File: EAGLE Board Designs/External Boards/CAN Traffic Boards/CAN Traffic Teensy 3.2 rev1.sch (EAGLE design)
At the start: 7 parts, among them X1 CONNECTOR-4NANO-FIT_RIGHT_ANG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

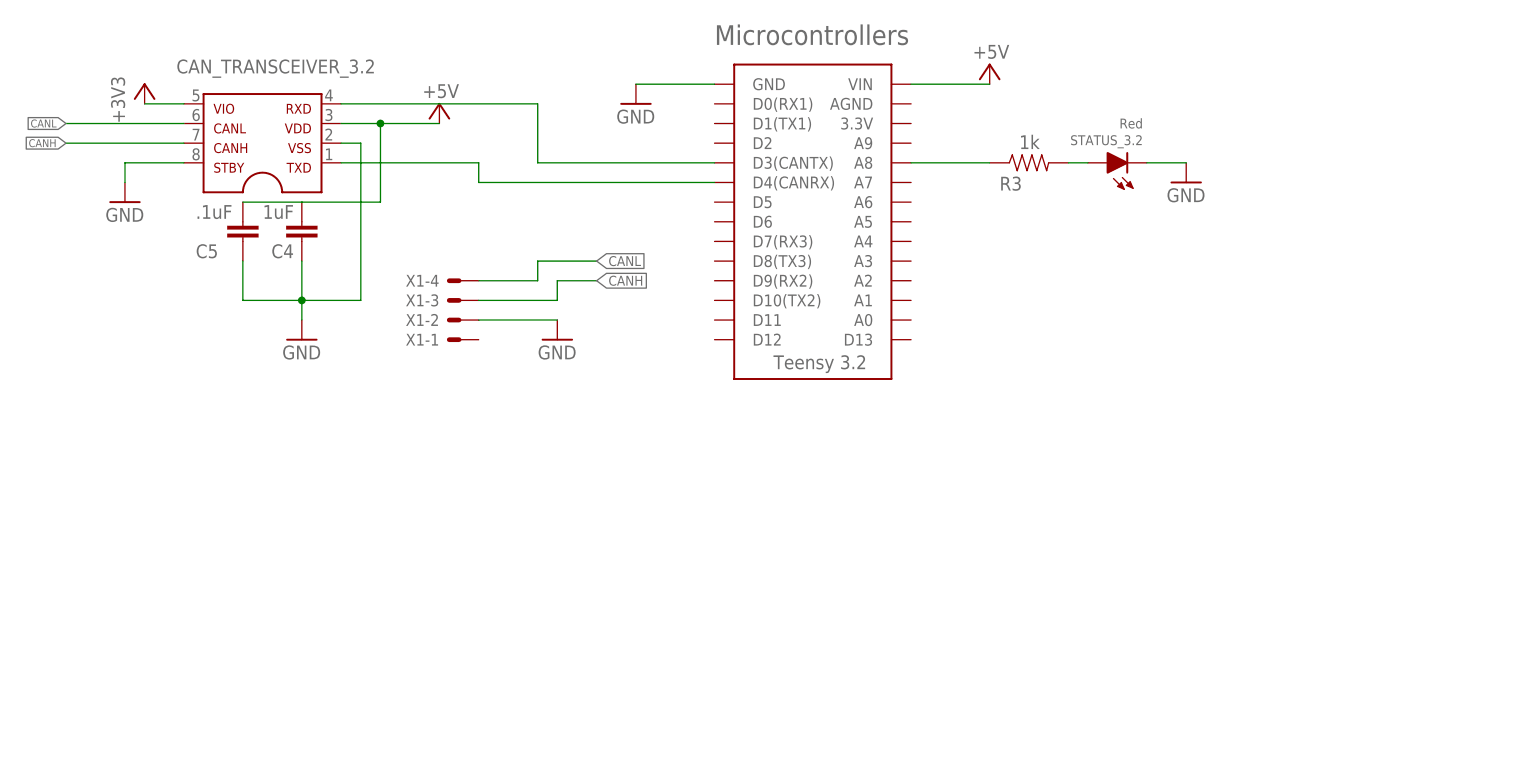
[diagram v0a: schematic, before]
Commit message: CAN Transceiver Boards
Added CAN Termination resistors, remade boards, added labels, put all LEDs on the same pin, added silksreens, and switched LED packages.
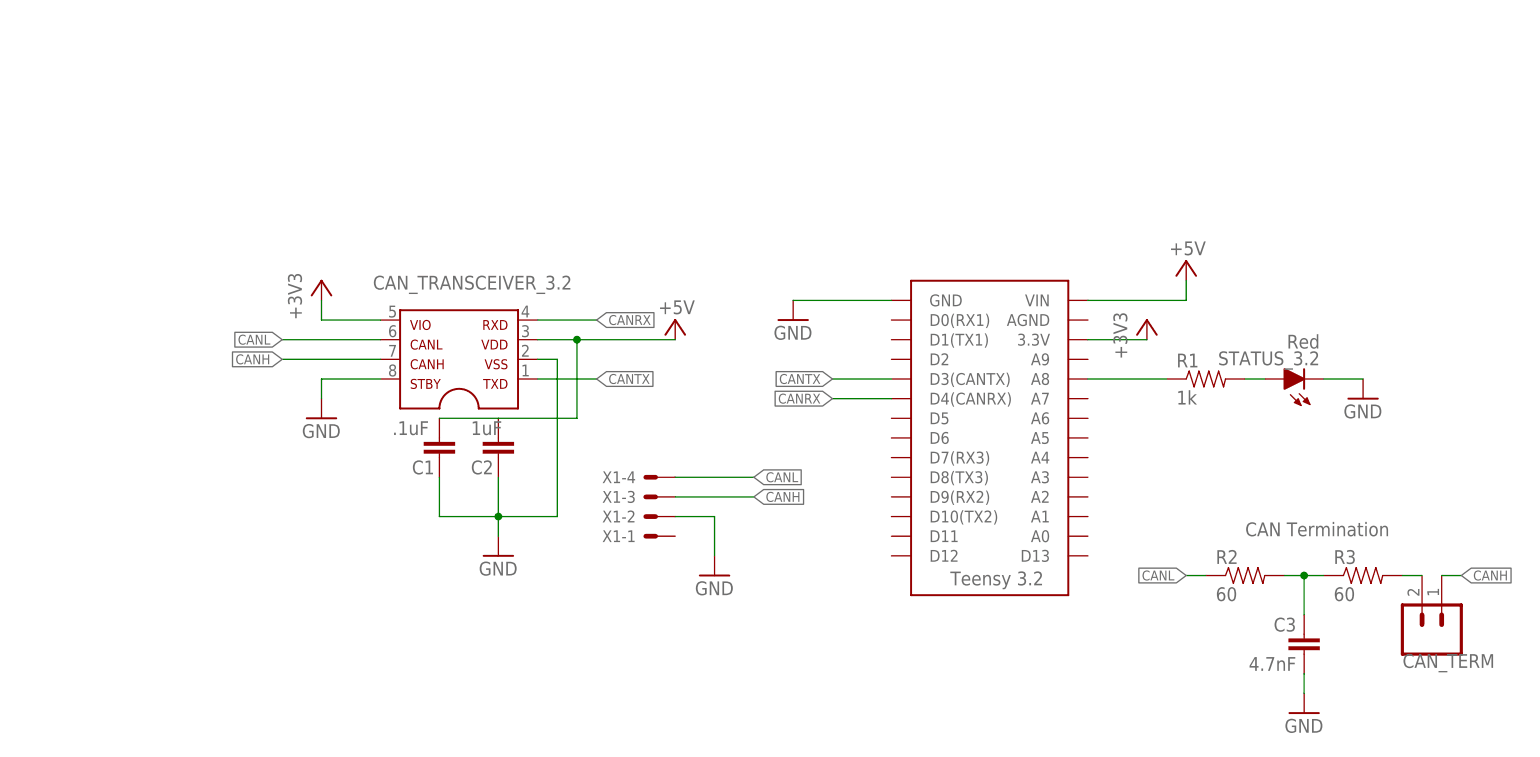
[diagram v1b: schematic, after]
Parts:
- removed C4: 1uF, HyTechDevices:CAP0603-CAP
- removed C5: .1uF, HyTechDevices:CAP0603-CAP
- removed U$1: TEENSY_3.2_SIMPLE, HyTechDevices:TEENSY_3.2_SIMPLE
- added 3.2: TEENSY_3.2_SIMPLE, HyTechDevices:TEENSY_3.2_SIMPLE
- added C1: .1uF, HyTechDevices:CAP0603-CAP
- added C2: 1uF, HyTechDevices:CAP0603-CAP
- added C3: 4.7nF, HyTechDevices:CAP0603-CAP
- added CAN_TERM: M02_SLIM, HyTechDevices:M02_SLIM
- added R1: 1k, HyTechDevices:RESISTOR0603-RES
- added R2: 60, HyTechDevices:RESISTOR0603-RES
- CAN_TRANSCEIVER_3.2: value MCP2562SOIC-08 -> MCP2562FDSOIC-08; device HyTechDevices:MCP2562SOIC-08 -> HyTechDevices:MCP2562FDSOIC-08
- R3: value 1k -> 60
- STATUS_3.2: device HyTechDevices:LED-0805 -> HyTechDevices:LED-0603
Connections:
- removed net N$1: R3.2, STATUS_3.2.A
- removed net N$10: CAN_TRANSCEIVER_3.2.4, U$1.D3(CANTX)
- removed net N$11: CAN_TRANSCEIVER_3.2.1, U$1.D4(CANRX)
- removed net N$7: R3.1, U$1.A8
- new net CANRX: 3.2.D4(CANRX), CAN_TRANSCEIVER_3.2.4
- new net CANTX: 3.2.D3(CANTX), CAN_TRANSCEIVER_3.2.1
- new net N$3: 3.2.A8, R1.1
- new net N$4: R1.2, STATUS_3.2.A
- new net N$5: CAN_TERM.2, R3.2
- net +3V3: now also 3.2.3.3V
- net +5V: now also 3.2.VIN, C1.1, C2.1; no longer C4.1, C5.1, U$1.VIN
- net CANH: now also CAN_TERM.1
- net CANL: now also R2.1
- net GND: now also 3.2.GND, C1.2, C2.2, C3.2, CAN_TRANSCEIVER_3.2.8; no longer C4.2, C5.2, U$1.GND
- net N$2: now also C3.1, R2.2, R3.1; no longer CAN_TRANSCEIVER_3.2.8
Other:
- note added: "CAN Termination"
- note removed: "Microcontrollers"
- moved on the sheet: CAN_TRANSCEIVER_3.2, R3, STATUS_3.2, X1-1, X1-2, X1-3, X1-4
